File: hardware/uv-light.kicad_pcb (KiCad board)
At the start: 2 copper layers, 25 x 15 mm, 15 parts, among them P1 CON-SENSOR, U1 M24C64, U2 Si1132, U3 DRILL, U4 DRILL, U5 DRILL, U6 DRILL

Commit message: add missing vcc connections
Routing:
- net VCC: track 25.9 -> 56.2 mm

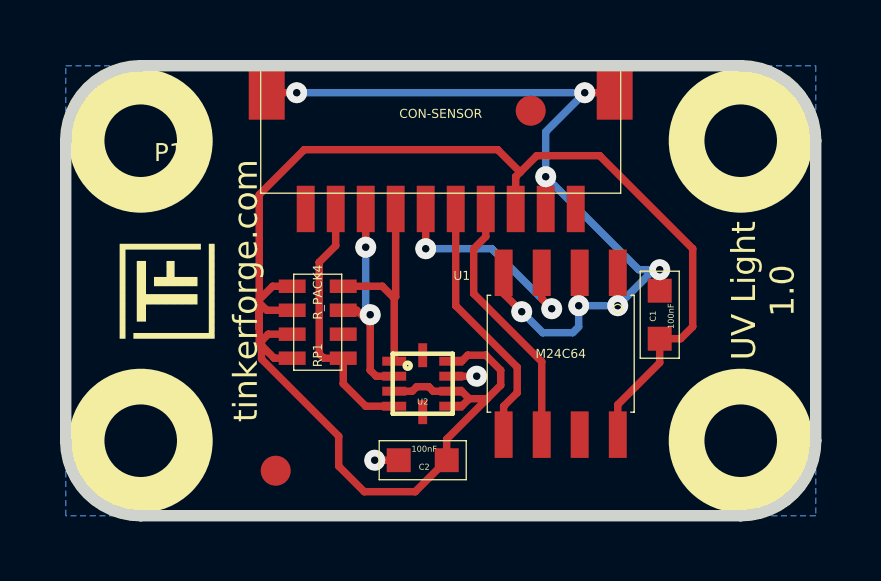
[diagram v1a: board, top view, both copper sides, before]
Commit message: change vcc routing
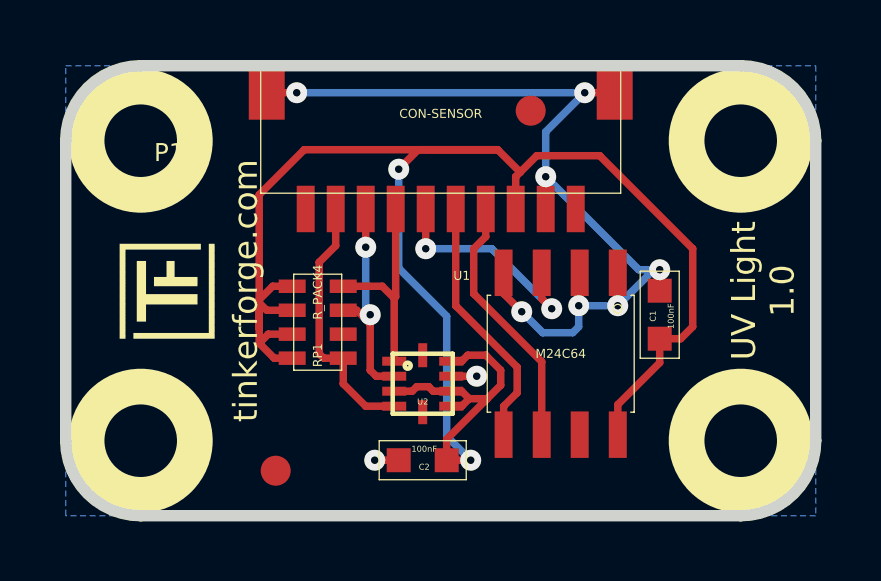
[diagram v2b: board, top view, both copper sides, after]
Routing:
- net VCC: track 56.2 -> 61.6 mm, vias 0 -> 2

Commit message: define pullup value
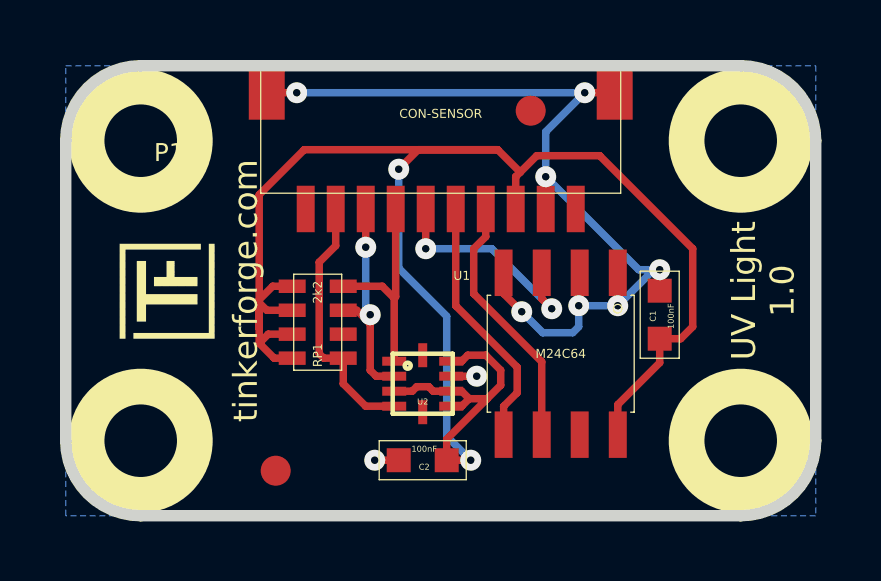
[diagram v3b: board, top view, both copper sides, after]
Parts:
- RP1: value R_PACK4 -> 2k2

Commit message: update to veml6070
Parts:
- added C3: 10µF, kicad-libraries:0603, F.Cu at (141.8, 100.2)
- added R1: 270k, kicad-libraries:0603, F.Cu at (138.1, 96.8)
- added R2: 10, kicad-libraries:0603, F.Cu at (138.9, 99.3)
- U2: value Si1132 -> VEML6070; footprint kicad-libraries:QFN-10 -> kicad-libraries:OPLGA6
- moved RP1 0.81 mm to (138.2, 94.2)
- moved C2 0.73 mm to (141.8, 98.9), turned to 180 degrees
- turned U2 to 180 degrees
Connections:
- C2 pad 2: VCC -> Net-(C2-Pad2)
- RP1 pad 7: Net-(P1-Pad8) -> Net-(P1-Pad7)
- RP1 pad 8: Net-(P1-Pad7) -> Net-(P1-Pad8)
- U2 pad 1: Net-(P1-Pad7) -> GND
- U2 pad 2: Net-(P1-Pad8) -> Net-(P1-Pad7)
- U2 pad 3: VCC -> Net-(P1-Pad8)
- U2 pad 4: Net-(P1-Pad9) -> Net-(R1-Pad1)
- U2 pad 5: (no net) -> Net-(P1-Pad9)
- U2 pad 6: VCC -> Net-(C2-Pad2)
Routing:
- net VCC: track 61.6 -> 40.9 mm, vias 2 -> 0
- net Net-(C2-Pad2): track 0.00 -> 4.83 mm
- net Net-(P1-Pad7): track 7.59 -> 11.7 mm, vias 0 -> 2
- net GND: track 33.4 -> 36.6 mm, vias 9 -> 10
- net Net-(P1-Pad6): track 7.69 -> 10.2 mm
- net Net-(R1-Pad1): track 0.00 -> 1.79 mm
- net Net-(P1-Pad9): track 8.78 -> 10.2 mm
- net Net-(P1-Pad8): track 8.03 -> 8.34 mm, vias 2 -> 0

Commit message: change resistor value to 240k
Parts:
- R1: value 270k -> 240k

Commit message: change resistor value back to 270k
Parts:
- R1: value 240k -> 270k

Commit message: Add 3d information (final)
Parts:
- C1, C2, C3: footprint kicad-libraries:0603 -> kicad-libraries:C0603
- R1, R2: footprint kicad-libraries:0603 -> kicad-libraries:R0603
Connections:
- P1 pad 1: (no net) -> Net-(P1-Pad1)
- P1 pad 10: (no net) -> Net-(P1-Pad10)
- RP1 pad 6: (no net) -> Net-(RP1-Pad6)
- U1 pad 7: (no net) -> Net-(U1-Pad7)
